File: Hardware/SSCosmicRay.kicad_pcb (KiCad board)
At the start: 2 copper layers, 80 x 50 mm, 47 parts, among them J3 CONN-9

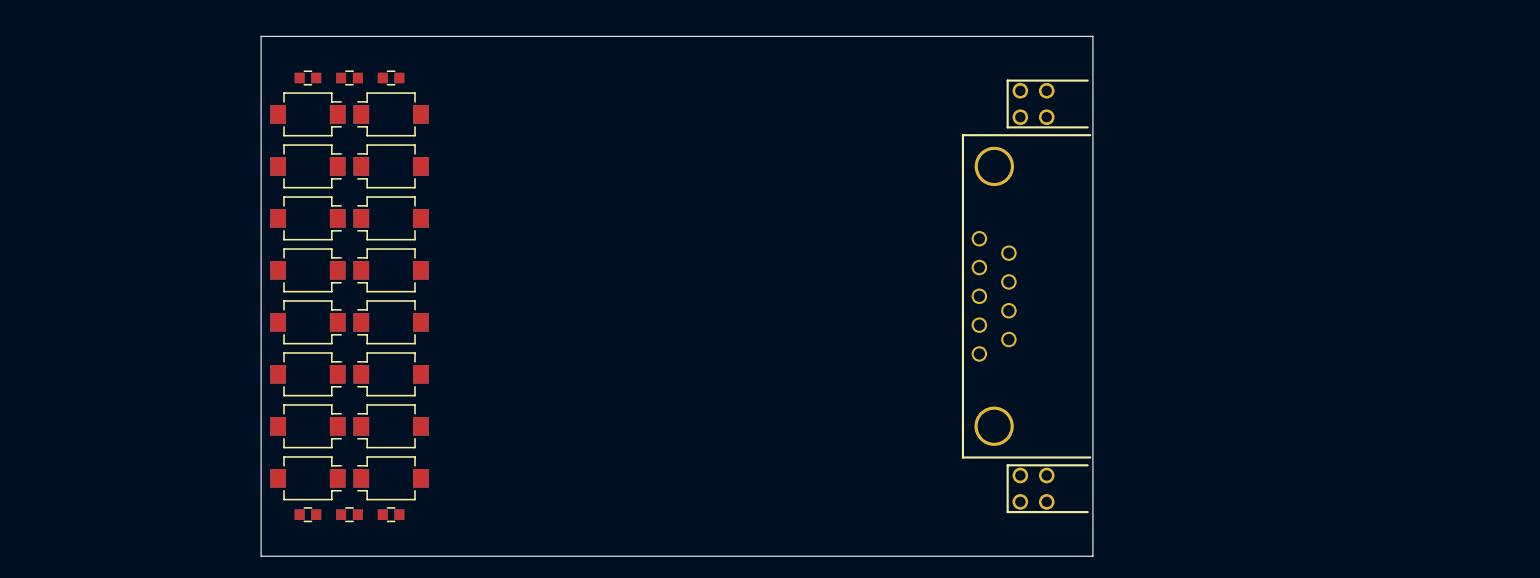
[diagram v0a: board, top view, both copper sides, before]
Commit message: Rough layout for pin map testing
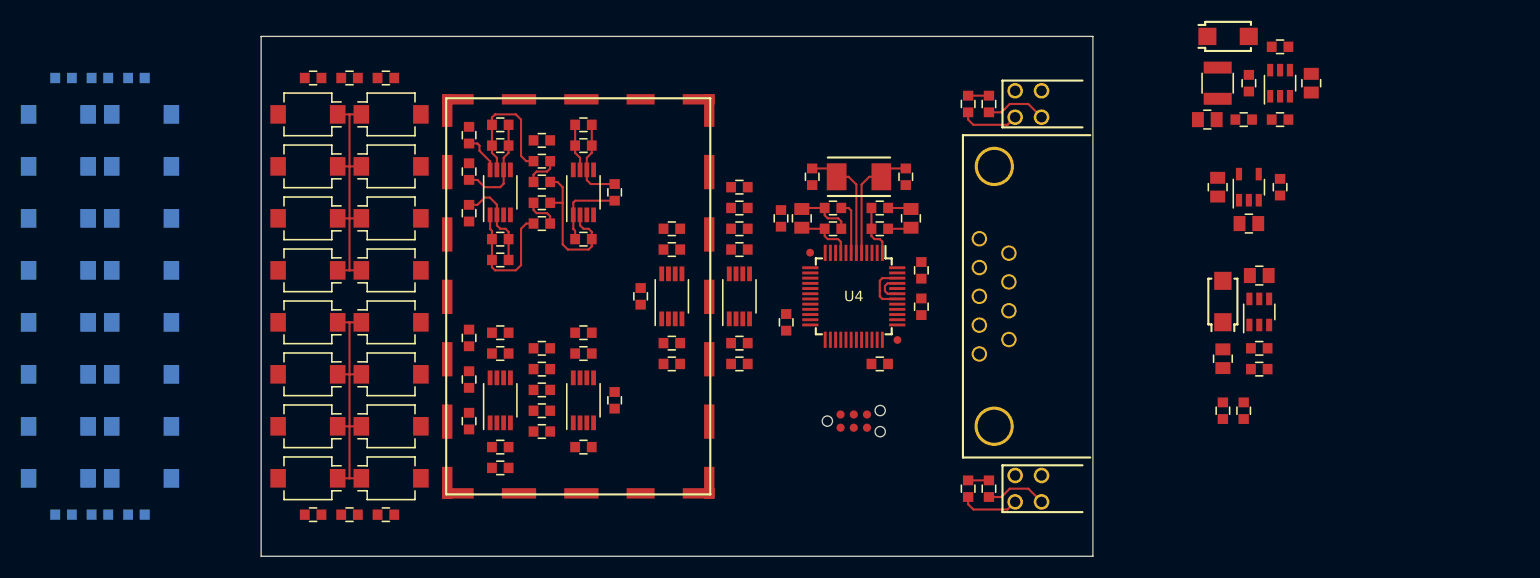
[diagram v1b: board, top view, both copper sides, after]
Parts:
- removed J3: CONN-9, CONN-TE-1734354
- added C10: 1000pF, CAPC1608-N, F.Cu at (154.0, 71.0)
- added C11: 1000pF, CAPC1608-N, F.Cu at (154.0, 65.0)
- added C12: 0.1uF, CAPC1608-N, F.Cu at (154.0, 63.0)
- added C13: 0.1uF, CAPC1608-N, F.Cu at (182.0, 71.5)
- added C14: 1uF, CAPC2012-N, F.Cu at (179.0, 70.5)
- added C15: 0.1uF, CAPC1608-N, F.Cu at (221.5, 89.0)
- added C16: 10uF, CAPC2012-N, F.Cu at (189.5, 70.5)
- added C17: 0.1uF, CAPC1608-N, F.Cu at (182.0, 69.5)
- added C18: 0.1uF, CAPC1608-N, F.Cu at (177.5, 80.5)
- added C19: 0.1uF, CAPC1608-N, F.Cu at (173.0, 82.5)
- added C2: 0.1uF, CAPC1608-N, F.Cu at (132.0, 57.0)
- added C20: 0.1uF, CAPC1608-N, F.Cu at (186.5, 84.5)
- added C21: 0.1uF, CAPC1608-N, F.Cu at (173.0, 73.5)
- added C23: 0.1uF, CAPC1608-N, F.Cu at (190.5, 75.5)
- added C24: 33pF, CAPC1608-N, F.Cu at (180.0, 66.5)
- added C25: 0.1uF, CAPC1608-N, F.Cu at (186.5, 69.5)
- added C26: 0.1uF, CAPC1608-N, F.Cu at (173.0, 69.5)
- added C27: 0.1uF, CAPC1608-N, B.Cu at (108.0, 57.0)
- added C28: 0.1uF, CAPC1608-N, B.Cu at (108.0, 99.0)
- added C29: 1000pF, CAPC1608-N, F.Cu at (158.0, 83.5)
- added C3: 1000pF, CAPC1608-N, F.Cu at (158.0, 63.5)
- added C31: 1000pF, CAPC1608-N, F.Cu at (147.0, 90.0)
- added C32: 1000pF, CAPC1608-N, F.Cu at (147.0, 86.0)
- added C33: C, CAPC1608-N, F.Cu at (150.0, 92.5)
- added C34: C, CAPC1608-N, F.Cu at (150.0, 83.5)
- added C35: 0.1uF, CAPC1608-N, F.Cu at (147.0, 82.0)
- added C36: 1000pF, CAPC1608-N, F.Cu at (154.0, 91.0)
- added C37: 1000pF, CAPC1608-N, F.Cu at (154.0, 85.0)
- added C38: 0.1uF, CAPC1608-N, F.Cu at (154.0, 83.0)
- added C39: 10uF, CAPC2012-N, F.Cu at (228.0, 57.5)
- added C4: 0.1uF, CAPC1608-N, F.Cu at (163.5, 78.0)
- added C40: 10uF, CAPC2012-N, F.Cu at (223.0, 76.0)
- added C41: 0.01uF, CAPC1608-N, F.Cu at (222.0, 57.5)
- added C42: 1uF, CAPC2012-N, F.Cu at (219.5, 84.0)
- added C43: 10uF, CAPC2012-N, F.Cu at (218.0, 61.0)
- added C44: 1uF, CAPC2012-N, F.Cu at (222.0, 71.0)
- added C5: 1000pF, CAPC1608-N, F.Cu at (147.0, 70.0)
- added C6: 1000pF, CAPC1608-N, F.Cu at (147.0, 66.0)
- added C7: C, CAPC1608-N, F.Cu at (150.0, 72.5)
- added C8: C, CAPC1608-N, F.Cu at (150.0, 63.5)
- added C9: 0.1uF, CAPC1608-N, F.Cu at (147.0, 62.5)
- added D17: LED-DUAL, LED-DUAL-VERT-300, F.Cu at (206.5, 96.5)
- added D36: CDBA140, SODFL5126-N, F.Cu at (219.5, 78.5)
- added FB1: FERRITE, INDC1608-N, F.Cu at (177.0, 70.5)
- added J1: ICSP-CORTEX, CONN-TC-2030-NL, F.Cu at (184.0, 90.0)
- added J2: CONN-9, CONN-TE-1734354, F.Cu at (207.0, 78.0)
- added L2: 10uH, INDC3225-N, F.Cu at (219.0, 57.5)
- added R10: 1M, RESC1608-N, F.Cu at (150.0, 61.5)
- added R11: 10k, RESC1608-N, F.Cu at (154.0, 69.0)
- added R12: 10k, RESC1608-N, F.Cu at (154.0, 67.0)
- added R14: 10k, RESC1608-N, F.Cu at (219.5, 89.0)
- added R15: 10k, RESC1608-N, F.Cu at (173.0, 67.5)
- added R16: 10k, RESC1608-N, F.Cu at (190.5, 79.0)
- added R17: 10k, RESC1608-N, F.Cu at (186.5, 71.5)
- added R18: 10k, RESC1608-N, F.Cu at (173.0, 84.5)
- added R19: 10k, RESC1608-N, F.Cu at (173.0, 71.5)
- added R2: 1M, RESC1608-N, F.Cu at (139.0, 57.0)
- added R21: 150, RESC1608-N, F.Cu at (197.0, 96.5)
- added R23: 150, RESC1608-N, F.Cu at (197.0, 59.5)
- added R25: 1M, RESC1608-N, B.Cu at (115.0, 99.0)
- added R26: 10M, RESC1608-N, B.Cu at (111.5, 57.0)
- added R27: 10M, RESC1608-N, B.Cu at (111.5, 99.0)
- added R28: 10k, RESC1608-N, F.Cu at (161.0, 88.0)
- added R29: 100k, RESC1608-N, F.Cu at (158.0, 81.5)
- added R30: 10k, RESC1608-N, F.Cu at (166.5, 84.5)
- added R31: 100k, RESC1608-N, F.Cu at (166.5, 82.5)
- added R32: 1M, RESC1608-N, F.Cu at (150.0, 94.5)
- added R33: 1M, RESC1608-N, F.Cu at (150.0, 81.5)
- added R34: 10k, RESC1608-N, F.Cu at (154.0, 89.0)
- added R35: 10k, RESC1608-N, F.Cu at (154.0, 87.0)
- added R36: 100k, RESC1608-N, F.Cu at (158.0, 92.5)
- added R37: 10k, RESC1608-N, F.Cu at (225.0, 54.0)
- added R38: R, RESC1608-N, F.Cu at (223.0, 85.0)
- added R4: 10M, RESC1608-N, F.Cu at (135.5, 57.0)
- added R41: 15.8k, RESC1608-N, F.Cu at (225.0, 61.0)
- added R5: 10k, RESC1608-N, F.Cu at (161.0, 68.0)
- added R6: 100k, RESC1608-N, F.Cu at (158.0, 61.5)
- added R7: 10k, RESC1608-N, F.Cu at (166.5, 71.5)
- added R8: 100k, RESC1608-N, F.Cu at (166.5, 73.5)
- added R9: 1M, RESC1608-N, F.Cu at (150.0, 74.5)
- added SH1: EMI, SHIELD-BMI-S-105, F.Cu at (157.5, 78.0)
- added U1: AD8616, SOP65P490-8N, F.Cu at (150.0, 68.0)
- added U10: TPS73130, SOT95P280-5N, F.Cu at (222.0, 67.5)
- added U2: AD8616, SOP65P490-8N, F.Cu at (158.0, 68.0)
- added U3: AD8616, SOP65P490-8N, F.Cu at (166.5, 78.0)
- added U4: STM32L151C6T6, QFP50P900X900-48N, F.Cu at (184.0, 78.0)
- added U5: LM2903DT, SOP65P490-8N, F.Cu at (173.0, 78.0)
- added U6: AD8616, SOP65P490-8N, F.Cu at (150.0, 88.0)
- added U7: AD8616, SOP65P490-8N, F.Cu at (158.0, 88.0)
- added U8: AOZ1280, SOT95P280-6N, F.Cu at (225.0, 57.5)
- added U9: MAX5026, SOT95P280-6N, F.Cu at (223.0, 79.5)
- added X1: 8MHz, XTAL-2SMD-60x35, F.Cu at (184.5, 66.5)
- C22: value 0.1uF -> 33pF; moved to F.Cu
- C46: value 0.1uF -> 1uF; footprint CAPC1608-N -> CAPC2012-N; moved to F.Cu
- D19: value LED-DUAL -> VBPW34FASR; footprint LED-DUAL-VERT-300 -> DIOC-BPW34R; moved to B.Cu
- D35: value VBPW34FASR -> CDBA140; footprint DIOC-BPW34R -> SODFL5126-N; moved to F.Cu
- R13: value 1M -> 100k
- R20, R22: value 1M -> 150; moved to F.Cu
- R24: value 10M -> 1M
- R39: value 10M -> R
- R40: value 10M -> 49.9k; moved to F.Cu
- moved D19 99.5 mm to (107.5, 60.5), turned to 0 degrees
- moved C45 94.1 mm to (225.0, 67.5), turned to 270 degrees
- moved R39 91.3 mm to (223.0, 83.0), turned to 0 degrees
- moved C46 88.1 mm to (219.0, 67.5), turned to 270 degrees
- moved R40 86.1 mm to (221.5, 61.0)
- moved D35 80.8 mm to (220.0, 53.0), turned to 0 degrees
- moved R20 68.1 mm to (195.0, 96.5), turned to 270 degrees
- moved R22 68.1 mm to (195.0, 59.5), turned to 270 degrees
- moved C22 66.0 mm to (189.0, 66.5), turned to 270 degrees
- moved R24 46.7 mm to (115.0, 57.0), turned to 0 degrees
- moved D18 37.0 mm to (206.5, 59.5)
- moved D23 33.5 mm to (107.5, 65.5), turned to 0 degrees
- moved D31 33.5 mm to (107.5, 75.5), turned to 0 degrees
- moved D27 32.0 mm to (107.5, 70.5), turned to 0 degrees
- moved D20 28.3 mm to (107.5, 80.5)
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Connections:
- C22 pad 1: N-00000104 -> /Processor/OSCI
- C45 pad 1: N-0000012 -> N-0000097
- C46 pad 1: N-0000097 -> VAA
- D18 pad 1: N-0000050 -> N-0000074
- D18 pad 4: GND -> (no net)
- D19 pad 1: N-0000045 -> GND
- D19 pad 2: (no net) -> /Detector 2/Det2A
- D20 pad 2: /Detector 2/Det2A -> /Detector 2/Det2B
- D21 pad 2: /Detector 2/Det2B -> /Detector 2/Det2A
- D22 pad 2: /Detector 2/Det2A -> /Detector 2/Det2B
- D23 pad 2: /Detector 2/Det2B -> /Detector 2/Det2A
- D24 pad 2: /Detector 2/Det2A -> /Detector 2/Det2B
- D25 pad 2: /Detector 2/Det2B -> /Detector 2/Det2A
- D26 pad 2: /Detector 2/Det2A -> /Detector 2/Det2B
- D27 pad 2: /Detector 2/Det2B -> /Detector 2/Det2A
- D28 pad 2: /Detector 2/Det2A -> /Detector 2/Det2B
- D29 pad 2: /Detector 2/Det2B -> /Detector 2/Det2A
- D30 pad 2: /Detector 2/Det2A -> /Detector 2/Det2B
- D31 pad 2: /Detector 2/Det2B -> /Detector 2/Det2A
- D32 pad 2: /Detector 2/Det2A -> /Detector 2/Det2B
- D33 pad 2: /Detector 2/Det2B -> /Detector 2/Det2A
- D34 pad 2: /Detector 2/Det2A -> /Detector 2/Det2B
- D35 pad 2: /Detector 2/Det2B -> /Power/Lx
- R1 pad 2: +12V -> VCOM
- R13 pad 1: N-0000012 -> N-000005
- R13 pad 2: +12V -> N-0000016
- R20 pad 1: N-0000097 -> +3.3V
- R20 pad 2: +12V -> N-0000076
- R22 pad 1: N-00000104 -> +3.3V
- R22 pad 2: +12V -> N-0000074
- R24 pad 1: N-00000104 -> N-0000095
- R24 pad 2: /Detector 2/Det2A -> VCOM
- R39 pad 1: N-0000012 -> GND
- R39 pad 2: /Detector 1/Det1B -> N-0000096
- R40 pad 1: N-0000097 -> N-00000100
- R40 pad 2: /Detector 2/Det2B -> +3.3V
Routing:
- net /Detector 1/Det1B: track 0.00 -> 24.1 mm
- net /Detector 1/Det1A: track 0.00 -> 24.1 mm
- net N-000005: track 0.00 -> 15.0 mm
- net N-0000012: track 0.00 -> 13.3 mm
- net N-0000010: track 0.00 -> 13.1 mm
- net /Processor/OSCO: track 0.00 -> 11.5 mm
- net /Processor/OSCI: track 0.00 -> 11.5 mm
- net N-0000013: track 0.00 -> 9.62 mm
- net N-0000011: track 0.00 -> 9.33 mm
- net N-000006: track 0.00 -> 8.35 mm
- net GND: track 0.00 -> 7.73 mm
- net N-0000016: track 0.00 -> 7.64 mm
- net +3.3V: track 0.00 -> 6.24 mm
- net N-0000073: track 0.00 -> 5.92 mm
- net N-0000075: track 0.00 -> 5.92 mm
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
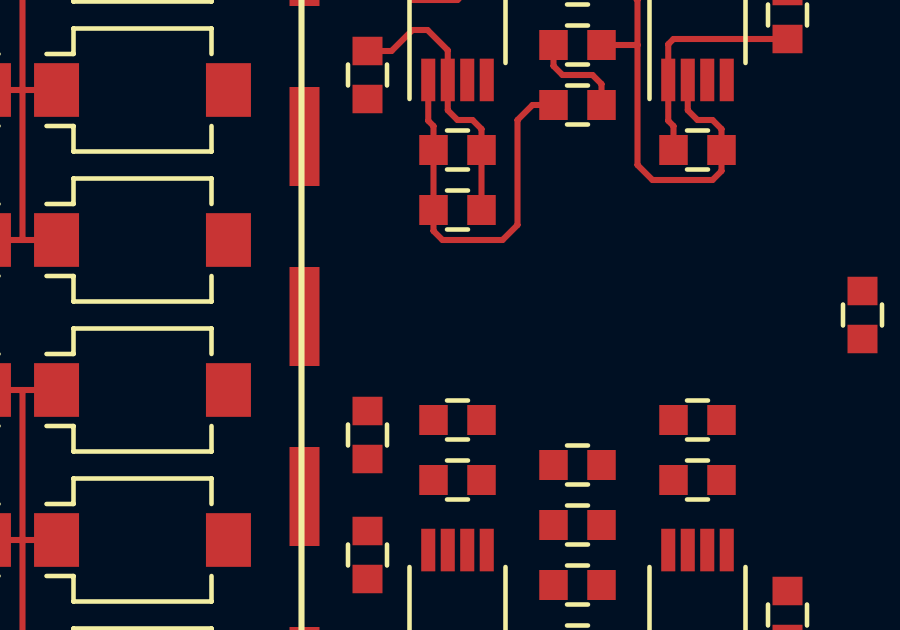
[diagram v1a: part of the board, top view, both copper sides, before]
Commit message: Add opamp reference voltage
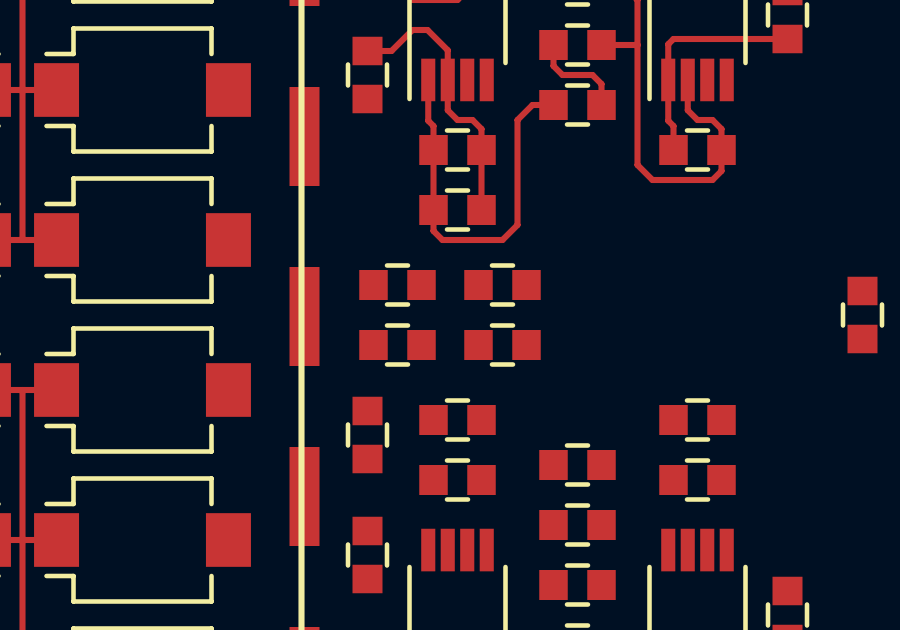
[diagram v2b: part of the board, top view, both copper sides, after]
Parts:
- added C30: 0.1uF, CAPC1608-N, F.Cu at (151.5, 79.0)
- added C47: 0.1uF, CAPC1608-N, F.Cu at (148.0, 77.0)
- added R42: 10k, RESC1608-N, F.Cu at (151.5, 77.0)
- added R43: 10k, RESC1608-N, F.Cu at (148.0, 79.0)
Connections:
- U3 pad 3: /Detector 2/Ref -> /Detector 1/Ref
- U6 pad 3: /Detector 2/Ref -> /Detector 1/Ref
- U6 pad 5: /Detector 2/Ref -> /Detector 1/Ref
- U7 pad 3: /Detector 2/Ref -> /Detector 1/Ref
- U7 pad 5: /Detector 2/Ref -> /Detector 1/Ref

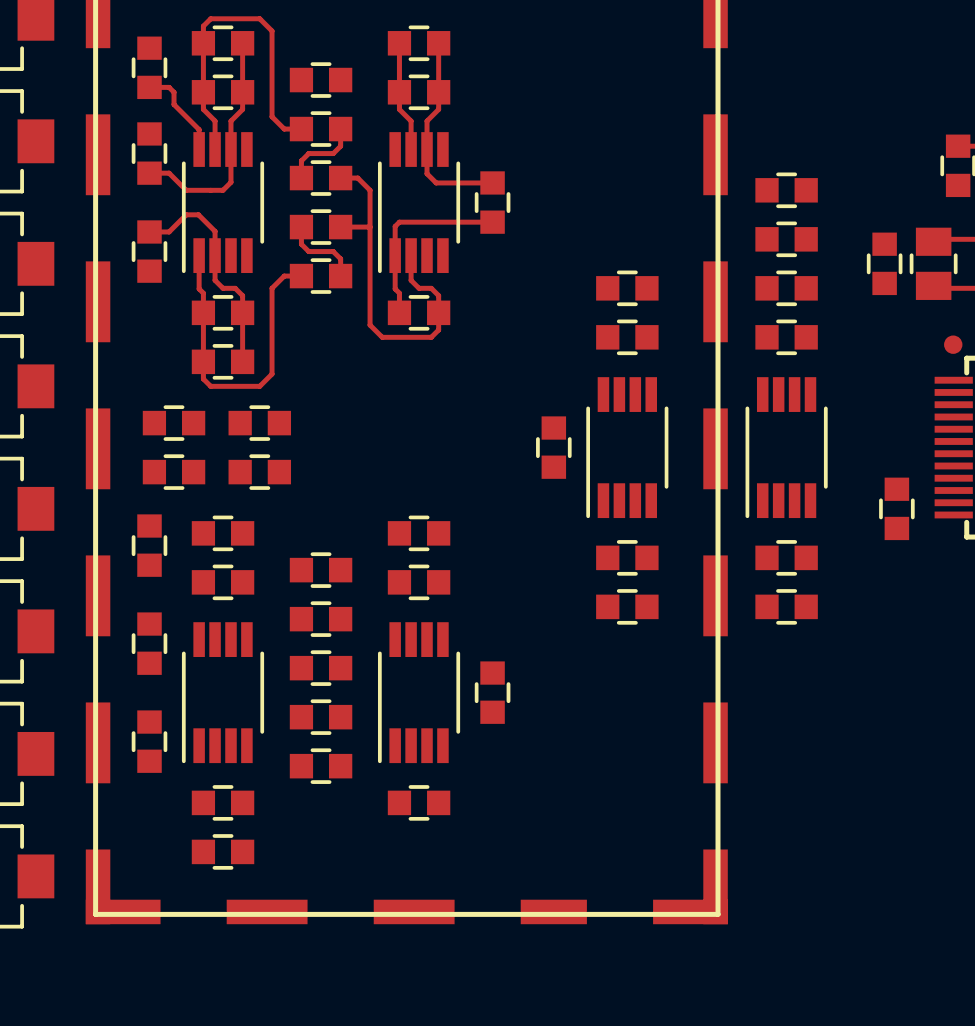
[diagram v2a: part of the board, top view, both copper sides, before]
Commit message: Change comparator label for better routing
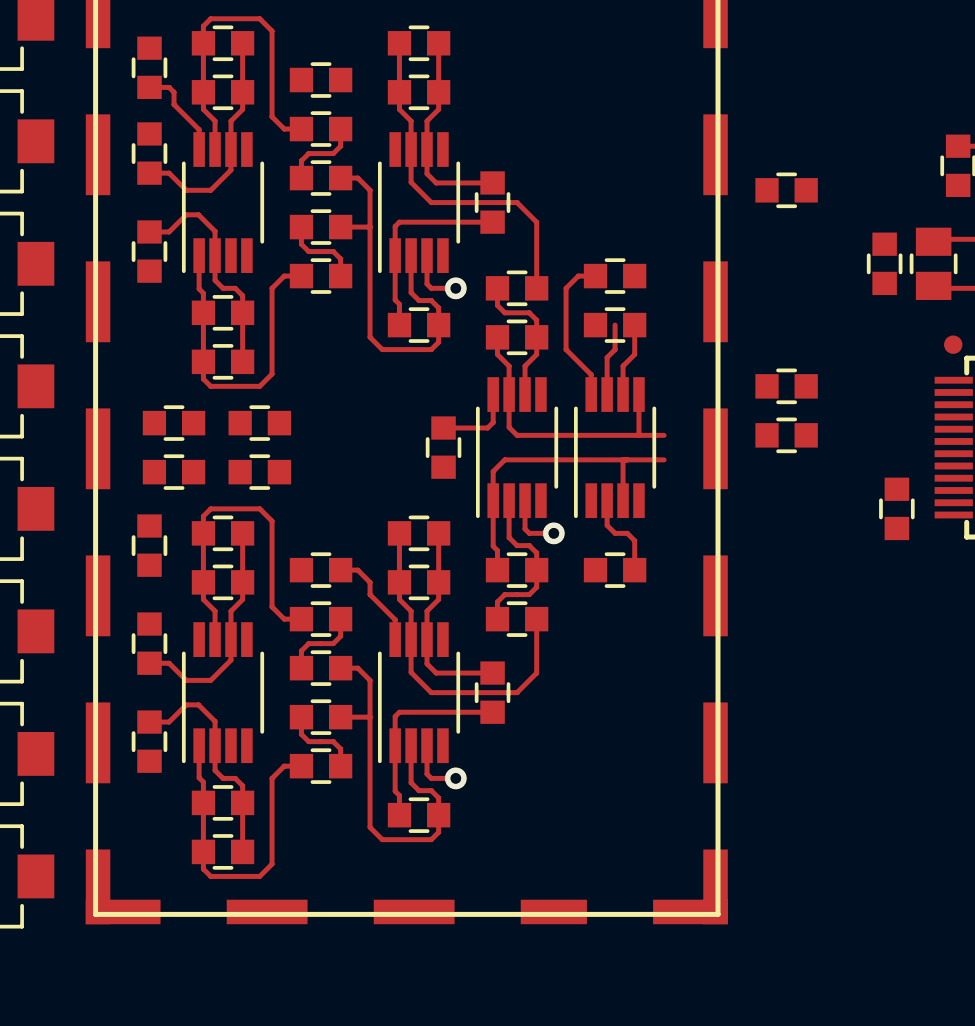
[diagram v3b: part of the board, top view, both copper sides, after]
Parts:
- moved C26 7.16 mm to (166.0, 71.0)
- moved C19 7.02 mm to (166.0, 83.0), turned to 180 degrees
- moved C21 7.02 mm to (166.0, 73.0), turned to 180 degrees
- moved R18 7.00 mm to (173.0, 77.5)
- moved U5 7.00 mm to (166.0, 78.0)
- moved R30 4.53 mm to (162.0, 85.0), turned to 0 degrees
- moved R31 4.53 mm to (162.0, 83.0)
- moved C4 4.50 mm to (159.0, 78.0)
- moved R7 4.50 mm to (162.0, 71.5), turned to 0 degrees
- moved R8 4.50 mm to (162.0, 73.5)
- moved U3 4.50 mm to (162.0, 78.0)
- moved R19 4.00 mm to (173.0, 75.5), turned to 180 degrees
- moved R13 0.50 mm to (158.0, 73.0)
- moved R36 0.50 mm to (158.0, 93.0)
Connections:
- R18 pad 2: /Processor/DET1 -> /Processor/DET2
- R19 pad 2: /Processor/DET2 -> /Processor/DET1
- U5 pad 1: /Processor/DET1 -> /Processor/DET2
- U5 pad 7: /Processor/DET2 -> /Processor/DET1
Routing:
- net N-0000086: track 0.00 -> 16.0 mm
- net N-0000088: track 0.00 -> 13.9 mm
- net N-0000081: track 0.00 -> 13.3 mm
- net N-0000089: track 0.00 -> 13.1 mm
- net /Processor/A2: track 0.00 -> 13.1 mm
- net /Processor/A1: track 0.00 -> 12.0 mm
- net N-0000011: track 4.53 -> 14.4 mm
- net N-0000085: track 0.00 -> 9.33 mm
- net N-0000091: track 0.00 -> 9.33 mm
- net N-0000080: track 0.00 -> 8.35 mm
- net N-0000084: track 0.00 -> 8.14 mm
- net VAA: track 3.84 -> 11.3 mm
- net /Detector 1/Ref: track 0.00 -> 7.22 mm, vias 0 -> 3
- net N-0000087: track 0.00 -> 6.84 mm
- net /Processor/THRSH: track 0.00 -> 6.63 mm
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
